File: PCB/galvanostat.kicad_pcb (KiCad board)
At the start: 2 copper layers, 86.4 x 61 mm, 27 parts, among them J0 Conn_01x02, J1 Conn_01x02, J2 Conn_01x02, U1 L7815, U2 LM358, U3 LM358, U4 LMC7660, U5 INA105KP, U6 LM358

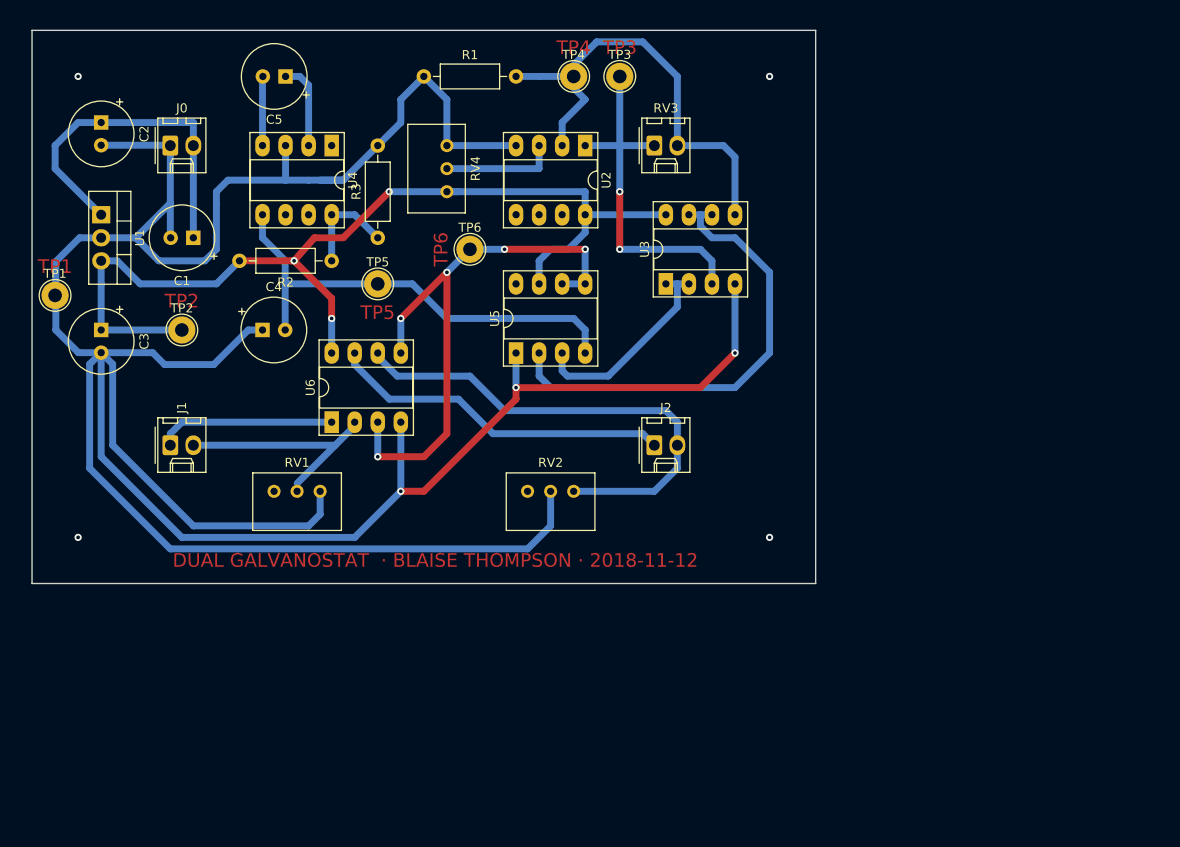
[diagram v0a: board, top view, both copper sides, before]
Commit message: dual to quad
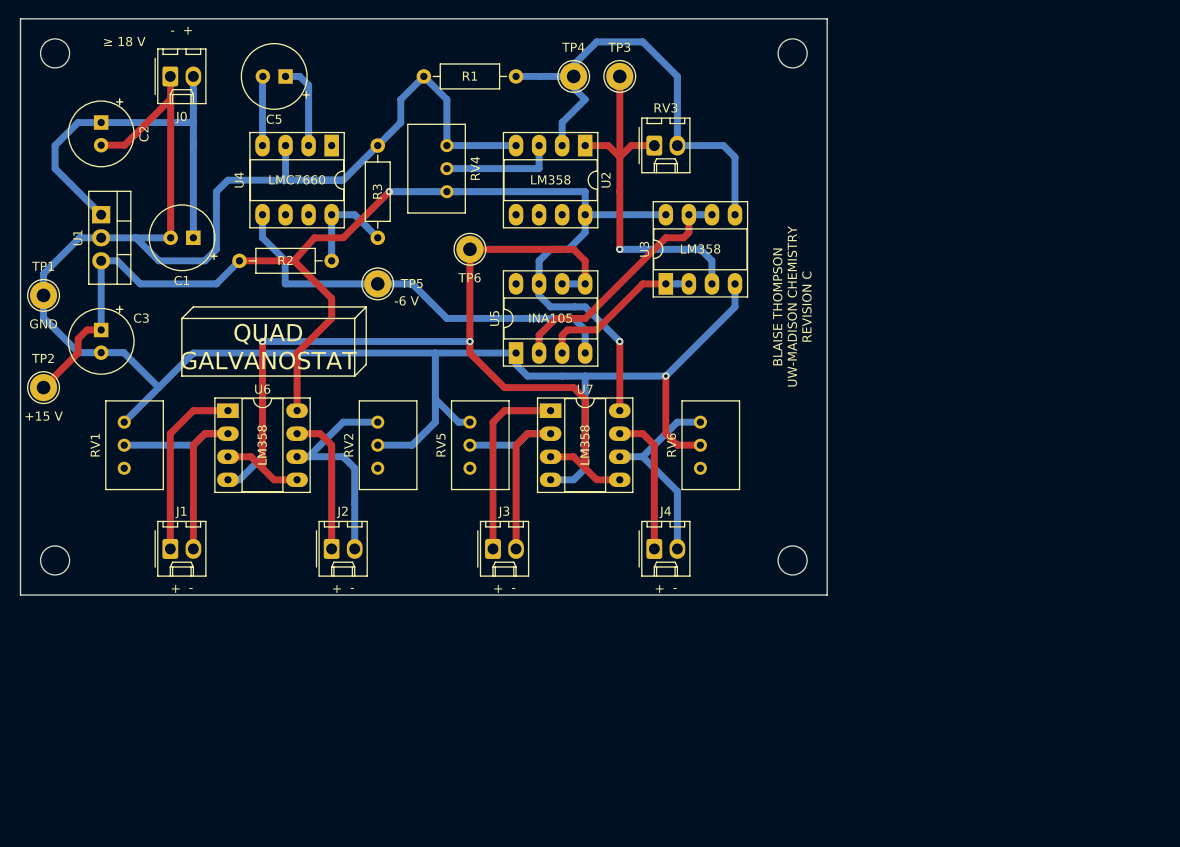
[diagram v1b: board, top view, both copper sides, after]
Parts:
- removed C4: 10uF, Capacitor_THT:CP_Radial_Tantal_D7.0mm_P2.50mm
- added J3: Conn_01x02, Connector_Molex:Molex_KK-254_AE-6410-02A_1x02_P2.54mm_Vertical, F.Cu at (121.9, 102.9)
- added J4: Conn_01x02, Connector_Molex:Molex_KK-254_AE-6410-02A_1x02_P2.54mm_Vertical, F.Cu at (139.7, 102.9)
- added REF**: MountingHole_3.2mm_M3, MountingHole:MountingHole_3.2mm_M3, F.Cu at (154.9, 104.1)
- added REF**: MountingHole_3.2mm_M3, MountingHole:MountingHole_3.2mm_M3, F.Cu at (73.7, 104.1)
- added REF**: MountingHole_3.2mm_M3, MountingHole:MountingHole_3.2mm_M3, F.Cu at (73.7, 48.3)
- added REF**: MountingHole_3.2mm_M3, MountingHole:MountingHole_3.2mm_M3, F.Cu at (154.9, 48.3)
- added RV5: 2kΩ, Potentiometer_THT:Potentiometer_Bourns_3299W_Vertical, F.Cu at (119.4, 88.9)
- added RV6: 2kΩ, Potentiometer_THT:Potentiometer_Bourns_3299W_Vertical, F.Cu at (144.8, 88.9)
- added U7: LM358, Package_DIP:DIP-8_W7.62mm_Socket_LongPads, F.Cu at (128.3, 87.6)
- R2, R3: value R_US -> 240Ω
- moved J2 37.4 mm to (104.1, 102.9)
- moved RV1 22.9 mm to (81.3, 88.9), turned to 90 degrees
- moved RV2 22.9 mm to (109.2, 88.9), turned to 90 degrees
- moved TP2 16.5 mm to (72.4, 85.1)
- moved U6 11.5 mm to (92.7, 87.6), turned to 0 degrees
- moved J1 11.4 mm to (86.4, 102.9)
- moved J0 7.62 mm to (86.4, 50.8)
- moved TP1 1.27 mm to (72.4, 74.9)
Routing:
- net GND: track 361.8 -> 272.8 mm, vias 3 -> 1
- net Net-(TP6-Pad1): track 63.9 -> 106.3 mm, vias 5 -> 2
- net +15V: track 110.7 -> 139.5 mm, vias 4 -> 2
- net Net-(J2-Pad2): track 54.0 -> 26.2 mm
- net Net-(J3-Pad2): track 0.00 -> 25.2 mm
- net Net-(U3-Pad6): track 52.5 -> 27.7 mm
- net Net-(J4-Pad2): track 0.00 -> 22.2 mm
- net Net-(J2-Pad1): track 38.0 -> 15.8 mm
- net Net-(J3-Pad1): track 0.00 -> 20.8 mm
- net Net-(J4-Pad1): track 0.00 -> 15.8 mm
- net Net-(C1-Pad1): track 38.9 -> 44.0 mm
- net -6V: track 51.4 -> 46.4 mm
- net Net-(U3-Pad1): track 23.1 -> 18.3 mm
- net Net-(J1-Pad2): track 25.0 -> 27.7 mm
- net Net-(RV3-Pad1): track 39.9 -> 40.9 mm, vias 2 -> 1
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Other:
- board size 86.4 x 61 mm -> 88.9 x 63.5 mm
- board text added: "+15 V"
- board text added: "- +"
- board text added: "-6 V"
- board text added: "BLAISE THOMPSON UW-MADISON CHEMISTRY REVISION C"
- board text added: "GND"
- board text added: "INA105"
- board text added: "LM358"
- board text added: "LMC7660"
- board text added: "QUAD GALVANOSTAT"
- board text added: "≥ 18 V"
- board text removed: "DUAL GALVANOSTAT · BLAISE THOMPSON · 2018-11-12"
- board text removed: "TP1"
- board text removed: "TP2"
- board text removed: "TP3"
- board text removed: "TP4"
- board text removed: "TP5"
- board text removed: "TP6"

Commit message: revision C
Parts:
- removed REF** (x4): MountingHole_3.2mm_M3, MountingHole:MountingHole_3.2mm_M3
- added C4: 10uF, Capacitor_THT:CP_Radial_Tantal_D7.0mm_P2.50mm, F.Cu at (144.8, 76.2)
- moved J4 44.7 mm to (176.5, 128.3)
- moved R3 44.7 mm to (146.1, 94.0)
- moved TP3 44.7 mm to (172.7, 76.2)
- moved TP5 44.7 mm to (146.1, 99.1)
- moved TP6 44.7 mm to (156.2, 95.2)
- moved U3 44.7 mm to (177.8, 99.1)
- moved C1 44.7 mm to (125.7, 94.0)
- moved C3 44.7 mm to (115.6, 104.1)
- moved J0 44.7 mm to (123.2, 76.2)
- moved J1 44.7 mm to (123.2, 128.3)
- moved J2 44.7 mm to (141.0, 128.3)
- moved J3 44.7 mm to (158.8, 128.3)
- moved R1 44.7 mm to (151.1, 76.2)
- moved RV2 44.7 mm to (146.1, 114.3)
- moved RV3 44.7 mm to (176.5, 83.8)
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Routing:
- net -6V: track 46.4 -> 70.4 mm
- net GND: track 272.8 -> 277.8 mm
